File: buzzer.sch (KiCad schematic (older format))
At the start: 7 parts, among them Q1 NPN, U8 CSS-0575A-SMT

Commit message: Start implementing new version: move USB port and altimeter module, new buzzer and volume control
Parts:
- removed Q1: NPN, buq2:SOT-23-3, symbol NPN
- removed SP1: SPEAKER, buq2:SPEAKER_240326000031, symbol SPEAKER
- removed U8: CSS-0575A-SMT, buq2:BUZZER-CUI-5MM, symbol CSS-0575A-SMT
- added C9: 100n, buq2:SM0603, symbol C
- added Q1: NPN-SOT23, buq2:SOT-23-3, symbol NPN-SOT23
- added U14: MCP4017, buq2:SC-70-6, symbol MCP4017
- added U8: SPEAKER-WITH-DUMMY, buq2:SPEAKER-T0825TR, symbol SPEAKER-WITH-DUMMY
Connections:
- net labels added: 3.3V, SCL, SDA
- wire segments 12 -> 11
- no-connect marks 0 -> 1
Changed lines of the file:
@@
 $EndDescr
-$Comp
-L CSS-0575A-SMT U8
-U 1 1 54464575
-P 6800 3650
-F 0 "U8" H 7050 3600 60  0000 C CNN
-F 1 "CSS-0575A-SMT" H 7150 4550 60  0000 C CNN
-F 2 "buq2:BUZZER-CUI-5MM" H 6800 3650 60  0001 C CNN
-F 3 "" H 6800 3650 60  0000 C CNN
-	1    6800 3650
-	1    0    0    -1
-$EndComp
-$Comp
-L NPN Q1
-U 1 1 5446457C
-P 5350 3650
-F 0 "Q1" H 5350 3500 50  0000 R CNN
-F 1 "NPN" H 5350 3800 50  0000 R CNN
-F 2 "buq2:SOT-23-3" H 5350 3650 60  0001 C CNN
-F 3 "" H 5350 3650 60  0000 C CNN
-	1    5350 3650
-	1    0    0    -1
-$EndComp
 $Comp
 L R R4
@@
 $EndComp
 Wire Wire Line
-	5800 3350 5800 3450
+	5800 3200 5800 3450
 Wire Wire Line
 	5800 3450 5450 3450
@@
 Text HLabel 5450 2900 1    60   Input ~ 0
 BATTERY
-Text HLabel 4650 3650 0    60   Input ~ 0
+Text HLabel 4600 3150 0    60   Input ~ 0
 BUZZER_DRIVE
 $Comp
@@
 	0    1    1    0
 $EndComp
-Wire Wire Line
-	6800 3350 5800 3350
 $Comp
 L R R8
@@
 	0    1    1    0
 $EndComp
-Wire Wire Line
-	6800 3050 6800 3200
 Text Notes 5650 2900 0    60   ~ 0
 two 0603 resistors as\npower dissipation is 0.2w
 $Comp
-L SPEAKER SP1
-U 1 1 54C7C4BE
-P 7250 4250
-F 0 "SP1" H 7150 4500 70  0000 C CNN
-F 1 "SPEAKER" H 7150 4000 70  0000 C CNN
-F 2 "buq2:SPEAKER_240326000031" H 7250 4250 60  0001 C CNN
-F 3 "http://media.digikey.com/pdf/Data%20Sheets/Knowles%20Acoustics%20PDFs/2403-260-00031.pdf" H 7250 4250 60  0001 C CNN
-	1    7250 4250
+L NPN-SOT23 Q1
+U 1 1 552EBAB2
+P 5450 3650
+F 0 "Q1" H 5330 3520 60  0000 C CNN
+F 1 "NPN-SOT23" H 5450 3350 60  0001 C CNN
+F 2 "buq2:SOT-23-3" H 5450 3650 60  0001 C CNN
+F 3 "" H 5450 3650 60  0000 C CNN
+	1    5450 3650
 	1    0    0    -1
 $EndComp
 Wire Wire Line
-	6800 3150 6650 3150
+	5250 3650 5150 3650
+$Comp
+L SPEAKER-WITH-DUMMY U8
+U 1 1 552EC00D
+P 6800 3550
+F 0 "U8" H 7050 3500 60  0000 C CNN
+F 1 "SPEAKER-WITH-DUMMY" H 7150 4450 60  0000 C CNN
+F 2 "buq2:SPEAKER-T0825TR" H 6800 3550 60  0001 C CNN
+F 3 "" H 6800 3550 60  0000 C CNN
+	1    6800 3550
+	1    0    0    -1
+$EndComp
 Wire Wire Line
-	6650 3150 6650 4150
+	6800 3200 5800 3200
+NoConn ~ 6800 3350
+$Comp
+L MCP4017 U14
+U 1 1 552EE006
+P 4250 3650
+F 0 "U14" H 4200 3350 60  0000 C CNN
+F 1 "MCP4017" H 4250 3950 60  0000 C CNN
+F 2 "buq2:SC-70-6" H 4200 3350 60  0001 C CNN
+F 3 "" H 4200 3350 60  0000 C CNN
+	1    4250 3650
+	1    0    0    -1
+$EndComp
 Wire Wire Line
-	6650 4150 6950 4150
-Connection ~ 6800 3150
+	4650 3550 4650 3150
 Wire Wire Line
-	6750 3350 6750 4350
+	4650 3150 4600 3150
+Text HLabel 3800 3550 0    60   Input ~ 0
+3.3V
+$Comp
+L GND #PWR028
+U 1 1 552EE2EB
+P 3700 3650
+F 0 "#PWR028" H 3700 3650 30  0001 C CNN
+F 1 "GND" H 3700 3580 30  0001 C CNN
+F 2 "" H 3700 3650 60  0000 C CNN
+F 3 "" H 3700 3650 60  0000 C CNN
+	1    3700 3650
+	0    1    1    0
+$EndComp
 Wire Wire Line
-	6750 4350 6950 4350
-Connection ~ 6750 3350
+	3700 3650 3800 3650
+Text HLabel 3800 3750 0    60   Input ~ 0
+SCL
+Text HLabel 4650 3750 3    60   Input ~ 0
+SDA
+$Comp
+L C C9
+U 1 1 552EE144
+P 3800 3350
+F 0 "C9" H 3800 3450 40  0000 L CNN
+F 1 "100n" H 3806 3265 40  0000 L CNN
+F 2 "buq2:SM0603" H 3838 3200 30  0001 C CNN
+F 3 "" H 3800 3350 60  0000 C CNN
+	1    3800 3350
+	1    0    0    -1
+$EndComp
+$Comp
+L GND #PWR029
+U 1 1 552EE1A7
+P 3800 3050
+F 0 "#PWR029" H 3800 3050 30  0001 C CNN
+F 1 "GND" H 3800 2980 30  0001 C CNN
+F 2 "" H 3800 3050 60  0000 C CNN
+F 3 "" H 3800 3050 60  0000 C CNN
+	1    3800 3050
+	-1   0    0    1
+$EndComp
+Wire Wire Line
+	3800 3050 3800 3150
 $EndSCHEMATC

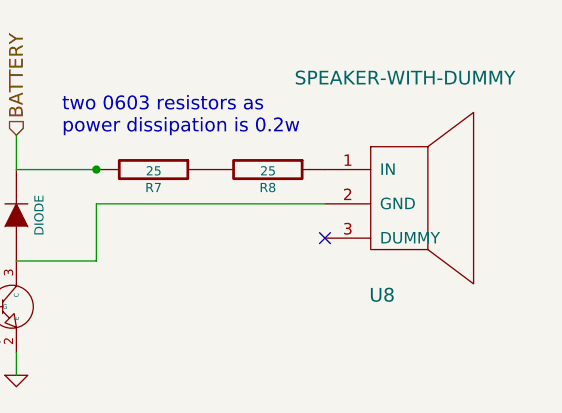
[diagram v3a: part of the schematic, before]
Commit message: Continuing laying out tracks
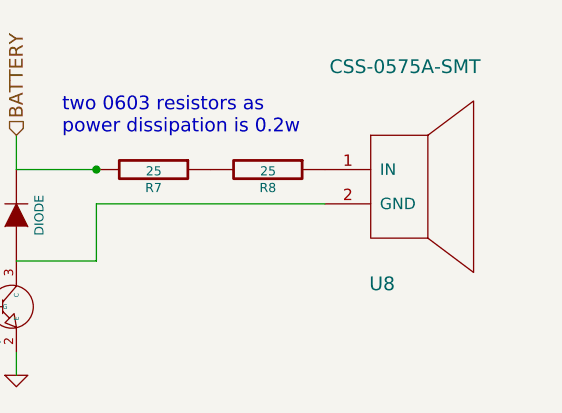
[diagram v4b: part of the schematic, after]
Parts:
- removed U8: SPEAKER-WITH-DUMMY, buq2:SPEAKER-T0825TR, symbol SPEAKER-WITH-DUMMY
- added U8: CSS-0575A-SMT, symbol CSS-0575A-SMT
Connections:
- net at D2.1 (A), Q1.3 (C): now also U8.2 (GND)
- net at R8.1: now also U8.1 (IN)
- no-connect marks 1 -> 0
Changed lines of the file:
@@
 $EndComp
 $Comp
-L GND #PWR027
+L GND #PWR27
 U 1 1 54464591
 P 5450 3950
-F 0 "#PWR027" H 5450 3950 30  0001 C CNN
+F 0 "#PWR27" H 5450 3950 30  0001 C CNN
 F 1 "GND" H 5450 3880 30  0001 C CNN
 F 2 "" H 5450 3950 60  0000 C CNN
@@
 Wire Wire Line
 	5250 3650 5150 3650
-$Comp
-L SPEAKER-WITH-DUMMY U8
-U 1 1 552EC00D
-P 6800 3550
-F 0 "U8" H 7050 3500 60  0000 C CNN
-F 1 "SPEAKER-WITH-DUMMY" H 7150 4450 60  0000 C CNN
-F 2 "buq2:SPEAKER-T0825TR" H 6800 3550 60  0001 C CNN
-F 3 "" H 6800 3550 60  0000 C CNN
-	1    6800 3550
-	1    0    0    -1
-$EndComp
 Wire Wire Line
 	6800 3200 5800 3200
-NoConn ~ 6800 3350
 $Comp
 L MCP4017 U14
@@
 3.3V
 $Comp
-L GND #PWR028
+L GND #PWR25
 U 1 1 552EE2EB
 P 3700 3650
-F 0 "#PWR028" H 3700 3650 30  0001 C CNN
+F 0 "#PWR25" H 3700 3650 30  0001 C CNN
 F 1 "GND" H 3700 3580 30  0001 C CNN
 F 2 "" H 3700 3650 60  0000 C CNN
@@
 $EndComp
 $Comp
-L GND #PWR029
+L GND #PWR26
 U 1 1 552EE1A7
 P 3800 3050
-F 0 "#PWR029" H 3800 3050 30  0001 C CNN
+F 0 "#PWR26" H 3800 3050 30  0001 C CNN
 F 1 "GND" H 3800 2980 30  0001 C CNN
 F 2 "" H 3800 3050 60  0000 C CNN
@@
 Wire Wire Line
 	3800 3050 3800 3150
+$Comp
+L CSS-0575A-SMT U8
+U 1 1 553133EC
+P 6800 3500
+F 0 "U8" H 7050 3450 60  0000 C CNN
+F 1 "CSS-0575A-SMT" H 7150 4400 60  0000 C CNN
+F 2 "" H 6800 3500 60  0000 C CNN
+F 3 "" H 6800 3500 60  0000 C CNN
+	1    6800 3500
+	1    0    0    -1
+$EndComp
 $EndSCHEMATC

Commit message: Some changes?
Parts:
- added L1: INDUCTOR, symbol INDUCTOR
- added P_AUD1: CONN_2, symbol CONN_2
- U8: footprint (none) -> buq2:BUZZER-CUI-5MM
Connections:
- net BATTERY: now also L1.1
- net at D2.1 (A), Q1.3 (C), U8.2 (GND): now also L1.2, P_AUD1.2 (PM)
- net at R8.1, U8.1 (IN): now also P_AUD1.1 (P1)
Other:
- note added: "For external speaker"
- note added: "Inductor is used to \ngenerate high voltage"
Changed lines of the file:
@@
 $Descr A4 11693 8268
 encoding utf-8
-Sheet 7 11
+Sheet 7 10
 Title ""
 Date ""
@@
 $EndComp
 $Comp
-L GND #PWR027
+L GND #PWR28
 U 1 1 54464591
 P 5450 3950
-F 0 "#PWR027" H 5450 3950 30  0001 C CNN
+F 0 "#PWR28" H 5450 3950 30  0001 C CNN
 F 1 "GND" H 5450 3880 30  0001 C CNN
 F 2 "" H 5450 3950 60  0000 C CNN
@@
 $EndComp
 Wire Wire Line
-	5800 3200 5800 3450
-Wire Wire Line
-	5800 3450 5450 3450
+	5800 3450 5800 3200
+Wire Wire Line
+	5100 3450 5800 3450
 Wire Wire Line
 	5800 3050 5450 3050
@@
 	5250 3650 5150 3650
 Wire Wire Line
-	6800 3200 5800 3200
+	5800 3200 6800 3200
 $Comp
 L MCP4017 U14
@@
 3.3V
 $Comp
-L GND #PWR028
+L GND #PWR11
 U 1 1 552EE2EB
 P 3700 3650
-F 0 "#PWR028" H 3700 3650 30  0001 C CNN
+F 0 "#PWR11" H 3700 3650 30  0001 C CNN
 F 1 "GND" H 3700 3580 30  0001 C CNN
 F 2 "" H 3700 3650 60  0000 C CNN
@@
 $EndComp
 $Comp
-L GND #PWR029
+L GND #PWR12
 U 1 1 552EE1A7
 P 3800 3050
-F 0 "#PWR029" H 3800 3050 30  0001 C CNN
+F 0 "#PWR12" H 3800 3050 30  0001 C CNN
 F 1 "GND" H 3800 2980 30  0001 C CNN
 F 2 "" H 3800 3050 60  0000 C CNN
@@
 F 0 "U8" H 7050 3450 60  0000 C CNN
 F 1 "CSS-0575A-SMT" H 7150 4400 60  0000 C CNN
-F 2 "" H 6800 3500 60  0000 C CNN
+F 2 "buq2:BUZZER-CUI-5MM" H 6800 3500 60  0001 C CNN
 F 3 "" H 6800 3500 60  0000 C CNN
 	1    6800 3500
 	1    0    0    -1
 $EndComp
+$Comp
+L CONN_2 P_AUD1
+U 1 1 56CE00DB
+P 7050 4000
+F 0 "P_AUD1" H 7177 4026 40  0000 L CNN
+F 1 "CONN_2" H 7177 3948 40  0000 L CNN
+F 2 "" H 7050 4000 60  0000 C CNN
+F 3 "" H 7050 4000 60  0000 C CNN
+	1    7050 4000
+	1    0    0    -1
+$EndComp
+Wire Wire Line
+	6700 3900 6700 3500
+Wire Wire Line
+	6700 3500 6800 3500
+Wire Wire Line
+	6800 3500 6800 3050
+Wire Wire Line
+	6700 4100 6500 4100
+Wire Wire Line
+	6500 4100 6500 3200
+Connection ~ 6500 3200
+Text Notes 7250 4200 0    60   ~ 0
+For external speaker
+$Comp
+L INDUCTOR L1
+U 1 1 56CE081B
+P 5100 3150
+F 0 "L1" H 5179 3189 40  0000 L CNN
+F 1 "INDUCTOR" H 5179 3111 40  0000 L CNN
+F 2 "" H 5100 3150 60  0000 C CNN
+F 3 "" H 5100 3150 60  0000 C CNN
+	1    5100 3150
+	1    0    0    -1
+$EndComp
+Connection ~ 5450 3450
+Wire Wire Line
+	5450 2950 5250 2950
+Wire Wire Line
+	5250 2950 5250 2850
+Wire Wire Line
+	5250 2850 5100 2850
+Connection ~ 5450 2950
+Text Notes 4150 2750 0    60   ~ 0
+Inductor is used to \ngenerate high voltage
 $EndSCHEMATC
